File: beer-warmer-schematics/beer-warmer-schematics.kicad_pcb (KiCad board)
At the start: 4 copper layers, 60 x 42.8 mm, 29 parts, among them J1 USB_C_Receptacle_USB2.0_14P, J2 Screw_Terminal_01x02, J3 Conn_01x07_Socket, J4 Conn_01x07_Socket, J5 Conn_01x04_Pin, J6 Screw_Terminal_01x03, Q1 AOD4184A, U2 LM2596S-5, U3 CH224K

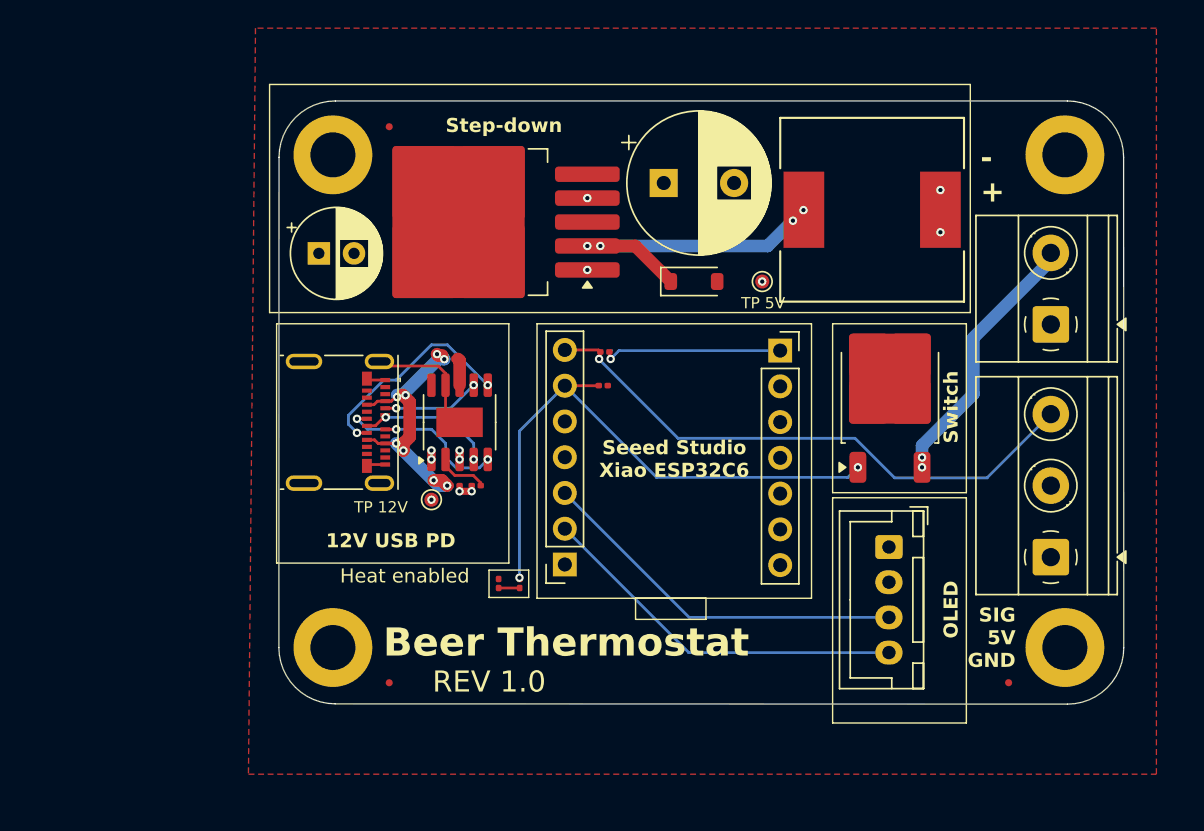
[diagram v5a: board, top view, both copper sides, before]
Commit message: power indicator
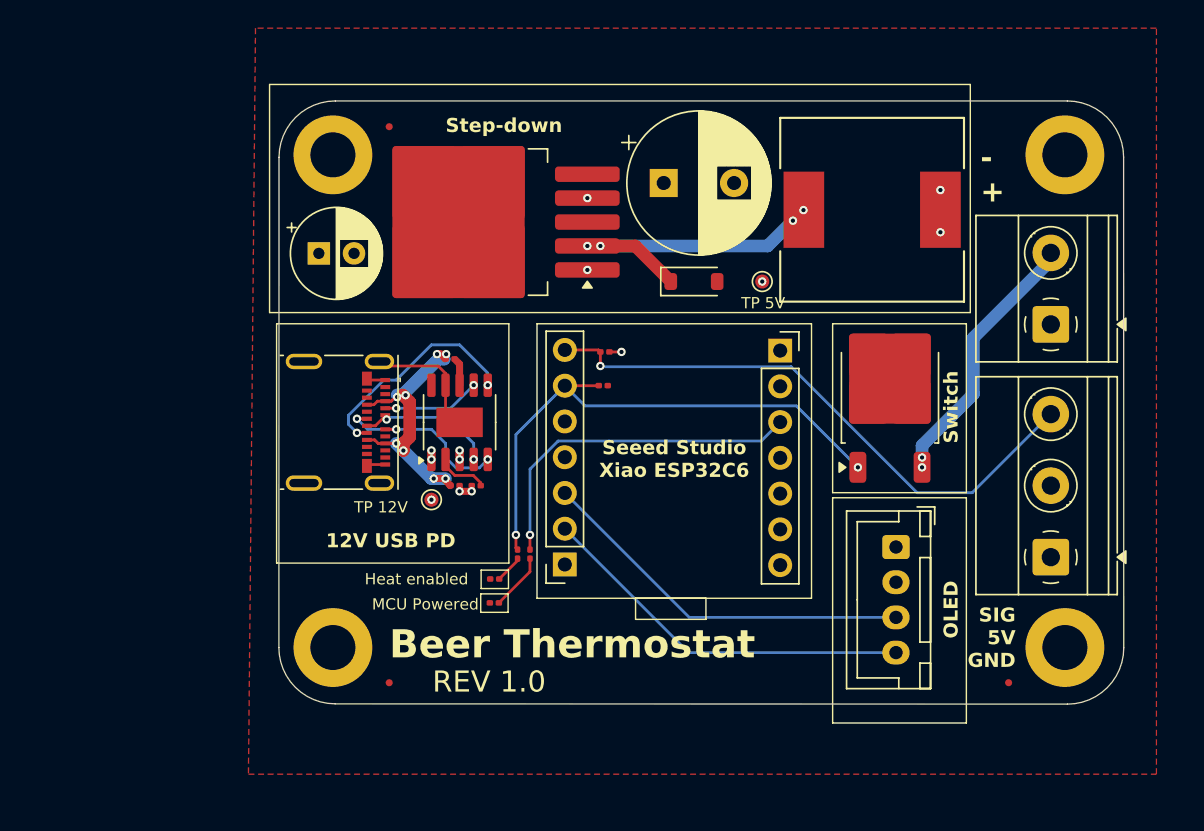
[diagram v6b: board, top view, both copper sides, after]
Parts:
- added D3: Red LED, Resistor_SMD:R_0201_0603Metric, F.Cu at (135.0, 106.8)
- added R6: 200R, Resistor_SMD:R_0201_0603Metric, F.Cu at (137.5, 103.4)
- moved R3 2.09 mm to (136.6, 103.4)
- moved J5 0.50 mm to (163.5, 102.9)
- moved D2 0.42 mm to (135.0, 105.1), turned to 0 degrees
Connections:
- J3 pad 3: Net-(J3-Pin_3) -> D3
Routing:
- net D3: track 0.00 -> 24.9 mm, vias 0 -> 1
- net +5V: track 12.9 -> 0.86 mm
- net Net-(D3-A): track 0.00 -> 4.06 mm
- net D1: track 41.2 -> 38.8 mm
- net D0: track 40.6 -> 41.6 mm
- net Net-(J1-VBUS-PadA4): track 21.2 -> 21.7 mm
- net Net-(J1-CC2): track 15.4 -> 15.9 mm
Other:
- board text added: "MCU Powered"

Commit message: use more standard components
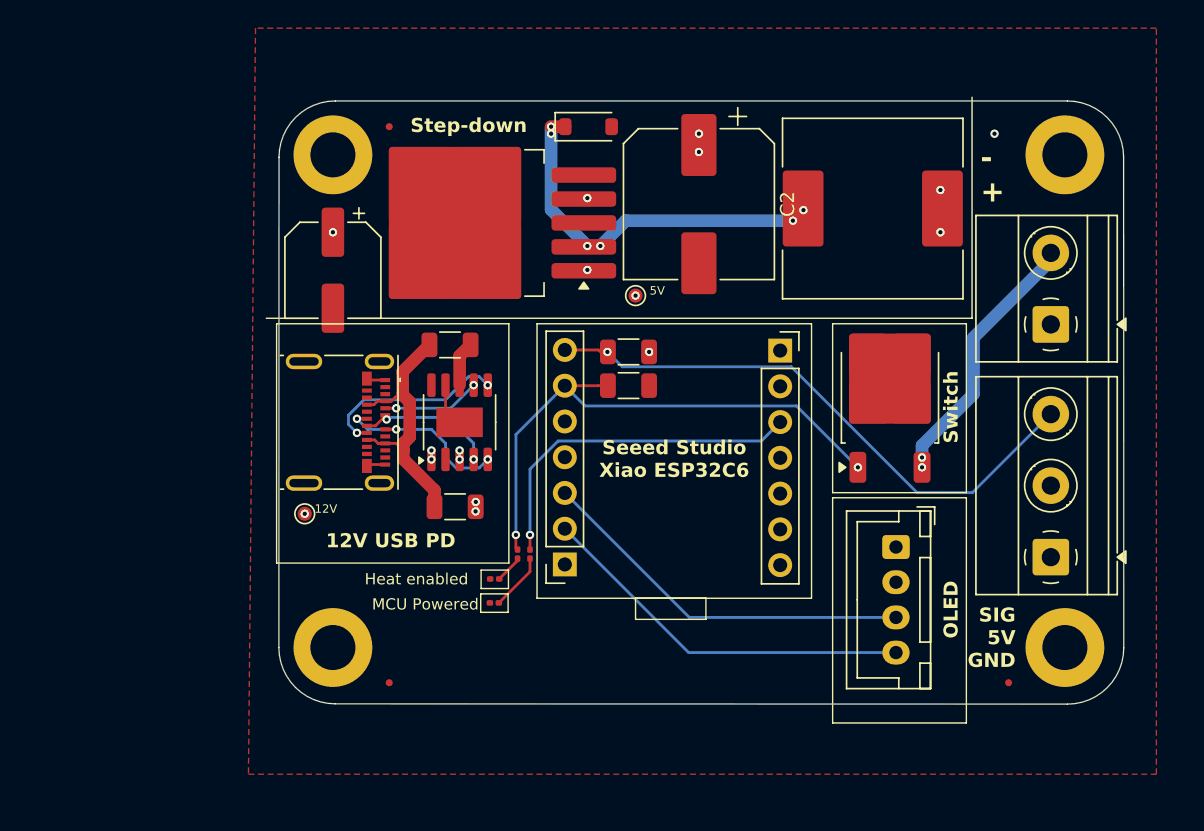
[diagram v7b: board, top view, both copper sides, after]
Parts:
- removed C1: 1uF, Capacitor_SMD:C_0201_0603Metric
- added kibuzzard-67EA8950: G***, kibuzzard-67EA8950, F.Cu at (142.5, 110.0)
- added kibuzzard-67EA89B2: G***, kibuzzard-67EA89B2, F.Cu at (145.4, 112.6)
- added kibuzzard-67EA89F2: G***, kibuzzard-67EA89F2, F.Cu at (134.5, 112.6)
- C2: footprint Capacitor_THT:CP_Radial_D10.0mm_P5.00mm -> Capacitor_SMD:CP_Elec_10x10.5
- C3: footprint Capacitor_THT:CP_Radial_D6.3mm_P2.50mm -> Capacitor_SMD:CP_Elec_6.3x7.7
- L1: footprint Library:IND_BOURNS_SRR1280 -> Inductor_SMD:L_SXN_SMDRI127
- R1, R2, R4, R5: footprint Resistor_SMD:R_0201_0603Metric -> Resistor_SMD:R_1206_3216Metric
- moved D1 13.3 mm to (141.7, 73.0)
- moved TP1 9.06 mm to (121.5, 100.5)
- moved TP2 9.06 mm to (145.0, 85.0)
- moved C2 2.92 mm to (149.5, 78.5), turned to -90 degrees
- moved R2 1.79 mm to (144.5, 91.4)
- moved R4 1.68 mm to (144.5, 89.0)
- moved C3 1.56 mm to (123.5, 83.2), turned to -90 degrees
- moved R1 1.50 mm to (132.2, 100.0)
- moved R5 1.00 mm to (131.8, 88.5)
- moved U2 0.26 mm to (133.7, 79.8)
- moved L1 0.10 mm to (161.9, 78.8)
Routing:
- net GND: track 15.3 -> 6.67 mm
- net Net-(D1-K): track 22.5 -> 27.0 mm, vias 4 -> 6
- net Net-(J1-VBUS-PadA4): track 21.7 -> 19.3 mm, vias 8 -> 0
- net Net-(J1-CC2): track 15.9 -> 13.5 mm
- net VDD: track 1.59 -> 0.00 mm, vias 8 -> 10
- net Net-(U3-VBUS): track 1.92 -> 3.19 mm
- net D0: track 41.6 -> 40.6 mm
- net +5V: track 0.86 -> 0.00 mm, vias 5 -> 7
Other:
- board text added: "12V"
- board text added: "5V"
- board text removed: "Beer Thermostat"
- board text removed: "REV 1.0"
- board text removed: "TP 12V"
- board text removed: "TP 5V"

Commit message: move extra tracks to other layer
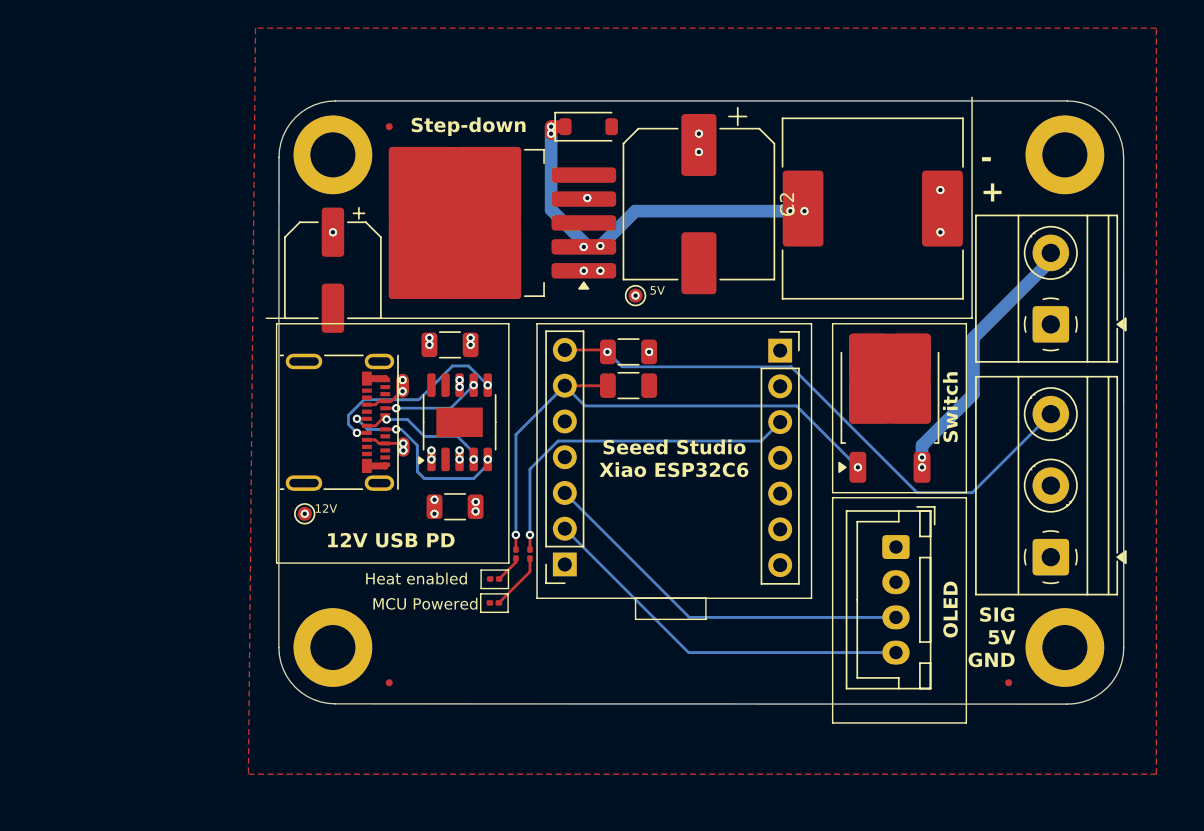
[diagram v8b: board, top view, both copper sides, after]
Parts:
- moved R3 0.12 mm to (136.5, 103.4)
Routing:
- net GND: track 6.67 -> 2.60 mm
- net Net-(J1-VBUS-PadA4): track 19.3 -> 21.0 mm, vias 0 -> 8
- net Net-(U3-DM): track 13.1 -> 14.4 mm
- net Net-(J1-CC2): track 13.5 -> 14.1 mm
- net Net-(U3-DP): track 9.74 -> 9.23 mm
- net Net-(U3-VBUS): track 3.19 -> 3.69 mm, vias 0 -> 4
- net D0: track 40.6 -> 41.1 mm
- net VDD: vias 10 -> 11
- net +5V: vias 7 -> 6
